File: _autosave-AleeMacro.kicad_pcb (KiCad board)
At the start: 2 copper layers, 245.1 x 103.6 mm, 67 parts, among them SW1 SW_Push, U1 ProMicro

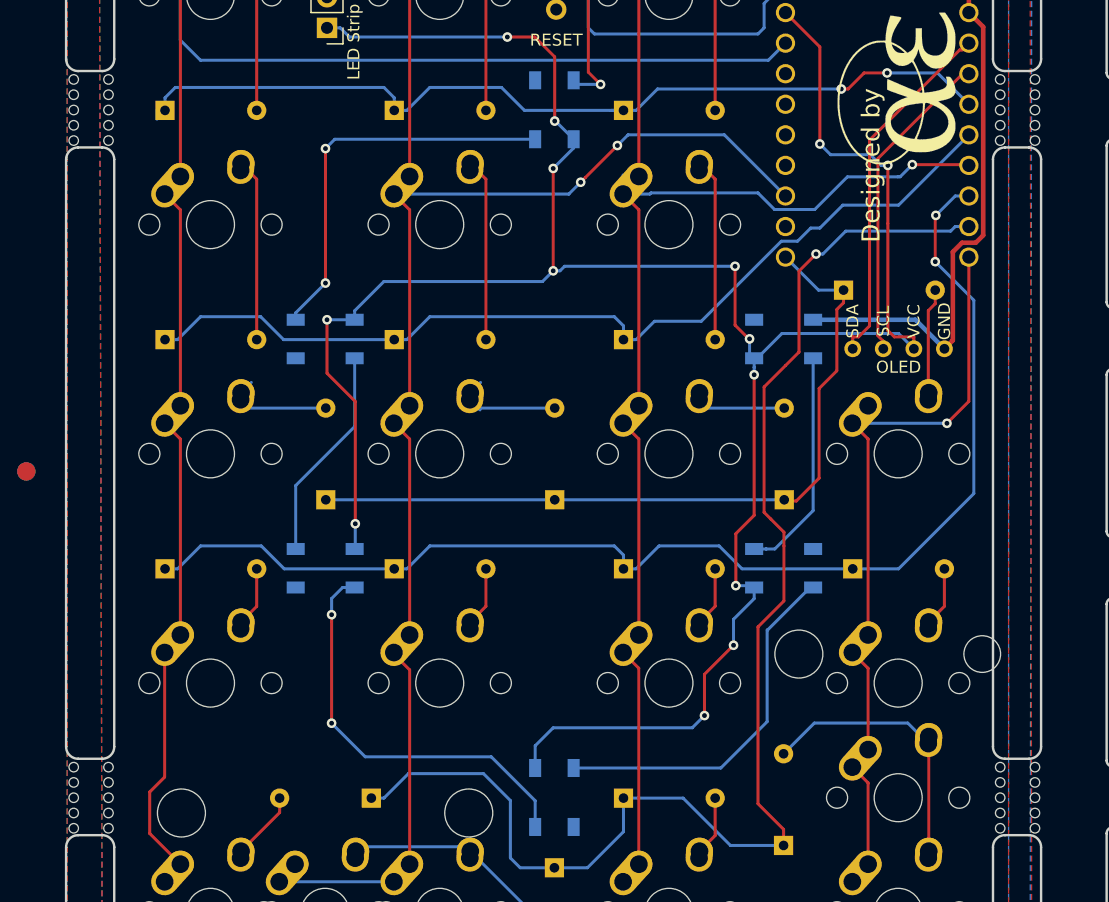
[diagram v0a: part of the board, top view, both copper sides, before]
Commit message: LEDS added
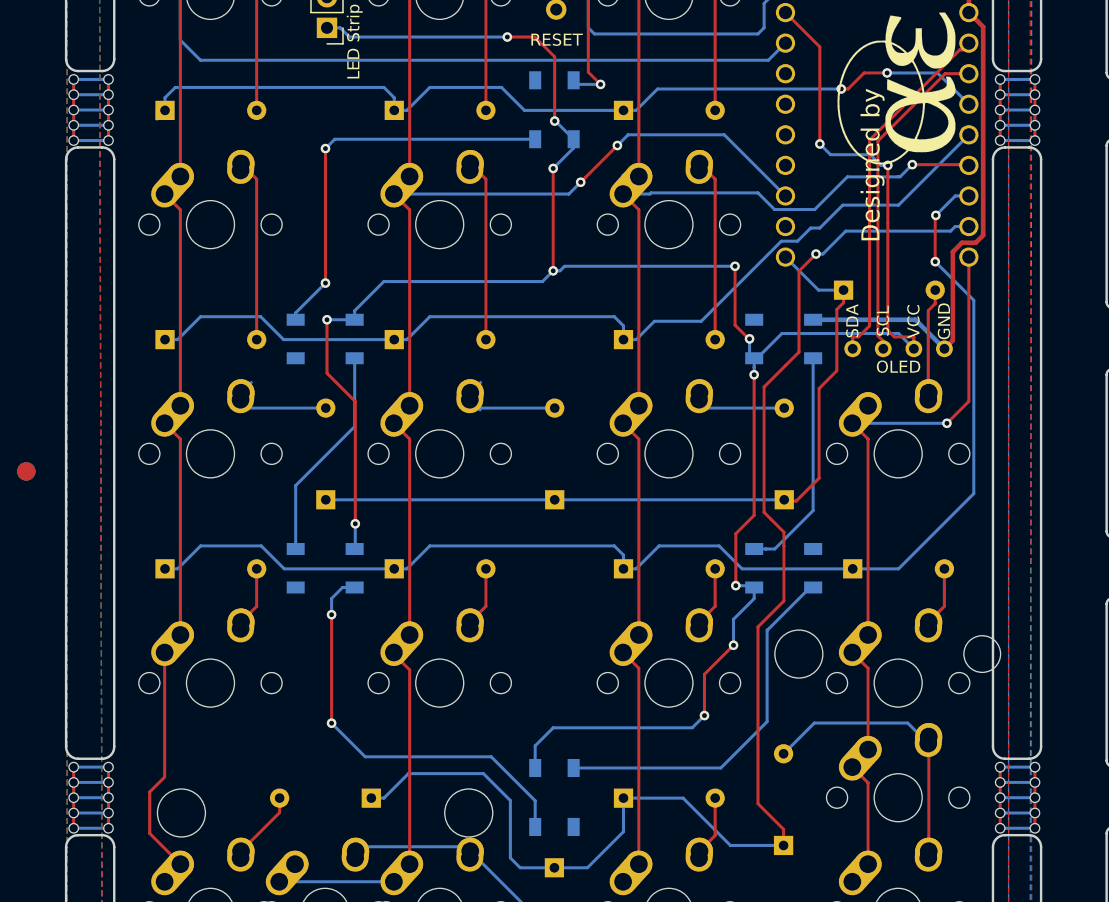
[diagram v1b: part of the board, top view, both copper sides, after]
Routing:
- net (no net): track 0.00 -> 98.4 mm
- net SCL: track 26.5 -> 27.8 mm
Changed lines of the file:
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@@
   (general
     (thickness 1.6)
-    (drawings 21)
-    (tracks 461)
+    (drawings 22)
+    (tracks 490)
     (zones 0)
     (modules 67)
@@
     (36 B.SilkS user)
     (37 F.SilkS user)
-    (38 B.Mask user)
-    (39 F.Mask user)
-    (40 Dwgs.User user)
+    (38 B.Mask user hide)
+    (39 F.Mask user hide)
+    (40 Dwgs.User user hide)
     (41 Cmts.User user)
     (42 Eco1.User user)
@@
     (pad "" np_thru_hole circle (at -2.54 -0.254 270) (size 0.7874 0.7874) (drill 0.7874) (layers *.Cu *.Mask))
   )
+  (gr_line (start 111.76 59.69) (end 112.014 59.69) (layer B.SilkS) (width 0.15))
   (gr_text "Designed by" (at 174.752 67.31 90) (layer F.SilkS)
     (effects (font (size 1.5 1.5) (thickness 0.3)))
@@
   (gr_line (start 184.94375 137.31875) (end 111.91875 137.31875) (layer Dwgs.User) (width 0.2))
   (gr_line (start 184.94375 45.24375) (end 184.94375 137.31875) (layer Dwgs.User) (width 0.2))
+  (segment (start 111.379 60.16625) (end 108.48975 60.16625) (width 0.25) (layer B.Cu) (net 0))
+  (segment (start 111.379 61.43625) (end 108.48975 61.43625) (width 0.25) (layer B.Cu) (net 0))
+  (segment (start 111.379 62.70625) (end 108.48975 62.70625) (width 0.25) (layer B.Cu) (net 0))
+  (segment (start 111.379 63.97625) (end 108.48975 63.97625) (width 0.25) (layer B.Cu) (net 0))
+  (segment (start 111.379 65.24625) (end 108.48975 65.24625) (width 0.25) (layer B.Cu) (net 0))
+  (segment (start 111.379 60.16625) (end 111.379 65.24625) (width 0.25) (layer F.Cu) (net 0))
+  (segment (start 108.48975 117.31625) (end 111.379 117.31625) (width 0.25) (layer B.Cu) (net 0))
+  (segment (start 108.48975 118.58625) (end 111.379 118.58625) (width 0.25) (layer B.Cu) (net 0))
+  (segment (start 108.48975 119.85625) (end 111.379 119.85625) (width 0.25) (layer B.Cu) (net 0))
+  (segment (start 108.48975 121.12625) (end 111.379 121.12625) (width 0.25) (layer B.Cu) (net 0))
+  (segment (start 108.48975 122.39625) (end 111.379 122.39625) (width 0.25) (layer B.Cu) (net 0))
+  (segment (start 111.379 122.39625) (end 111.379 117.31625) (width 0.25) (layer F.Cu) (net 0))
+  (segment (start 108.48975 117.31625) (end 108.48975 122.39625) (width 0.25) (layer F.Cu) (net 0))
+  (segment (start 185.4835 117.31625) (end 185.4835 122.39625) (width 0.25) (layer F.Cu) (net 0))
+  (segment (start 188.37275 117.31625) (end 188.37275 122.39625) (width 0.25) (layer F.Cu) (net 0))
+  (segment (start 185.4835 122.39625) (end 188.37275 122.39625) (width 0.25) (layer B.Cu) (net 0))
+  (segment (start 185.4835 121.12625) (end 188.37275 121.12625) (width 0.25) (layer B.Cu) (net 0))
+  (segment (start 185.4835 119.85625) (end 188.37275 119.85625) (width 0.25) (layer B.Cu) (net 0))
+  (segment (start 185.4835 118.58625) (end 188.37275 118.58625) (width 0.25) (layer B.Cu) (net 0))
+  (segment (start 185.4835 117.31625) (end 188.37275 117.31625) (width 0.25) (layer B.Cu) (net 0))
+  (segment (start 185.4835 65.24625) (end 188.37275 65.24625) (width 0.25) (layer B.Cu) (net 0))
+  (segment (start 185.4835 63.97625) (end 188.37275 63.97625) (width 0.25) (layer B.Cu) (net 0))
+  (segment (start 185.4835 62.70625) (end 188.37275 62.70625) (width 0.25) (layer B.Cu) (net 0))
+  (segment (start 185.4835 61.43625) (end 188.37275 61.43625) (width 0.25) (layer B.Cu) (net 0))
+  (segment (start 185.4835 60.16625) (end 188.37275 60.16625) (width 0.25) (layer B.Cu) (net 0))
+  (segment (start 188.37275 60.16625) (end 188.37275 65.24625) (width 0.25) (layer F.Cu) (net 0))
+  (segment (start 185.4835 60.16625) (end 185.4835 65.24625) (width 0.25) (layer F.Cu) (net 0))
+  (segment (start 108.48975 65.24625) (end 108.48975 60.16625) (width 0.25) (layer F.Cu) (net 0))
   (segment (start 123.03125 48.73625) (end 122.39625 48.10125) (width 0.25) (layer F.Cu) (net 1))
   (segment (start 122.97625 48.68125) (end 122.35625 48.68125) (width 0.25) (layer F.Cu) (net 1))
@@
   (segment (start 174.625 80.645) (end 174.625 65.2145) (width 0.25) (layer F.Cu) (net 31))
   (segment (start 182.372 59.69) (end 182.88 59.69) (width 0.25) (layer F.Cu) (net 32))
+  (segment (start 180.9115 59.69) (end 182.88 59.69) (width 0.25) (layer F.Cu) (net 32))
+  (segment (start 175.3235 65.278) (end 180.9115 59.69) (width 0.25) (layer F.Cu) (net 32))
+  (segment (start 175.3235 81.4705) (end 175.3235 65.278) (width 0.25) (layer F.Cu) (net 32))
   (segment (start 175.768 82.55) (end 175.768 81.915) (width 0.25) (layer F.Cu) (net 32))
-  (segment (start 175.3235 81.4705) (end 175.3235 66.7385) (width 0.25) (layer F.Cu) (net 32))
   (segment (start 175.768 81.915) (end 175.3235 81.4705) (width 0.25) (layer F.Cu) (net 32))
-  (segment (start 175.3235 66.7385) (end 182.372 59.69) (width 0.25) (layer F.Cu) (net 32))
   (segment (start 165.2876 83.3372) (end 167.3448 81.28) (width 0.25) (layer B.Cu) (net 33))
   (segment (start 177.038 81.28) (end 178.308 82.55) (width 0.25) (layer B.Cu) (net 33))
